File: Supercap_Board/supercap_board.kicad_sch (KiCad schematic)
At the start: 15 parts, among them Q10 2SCR587D3, Q11 2SAR587D3, U18 TLV9301xDBV

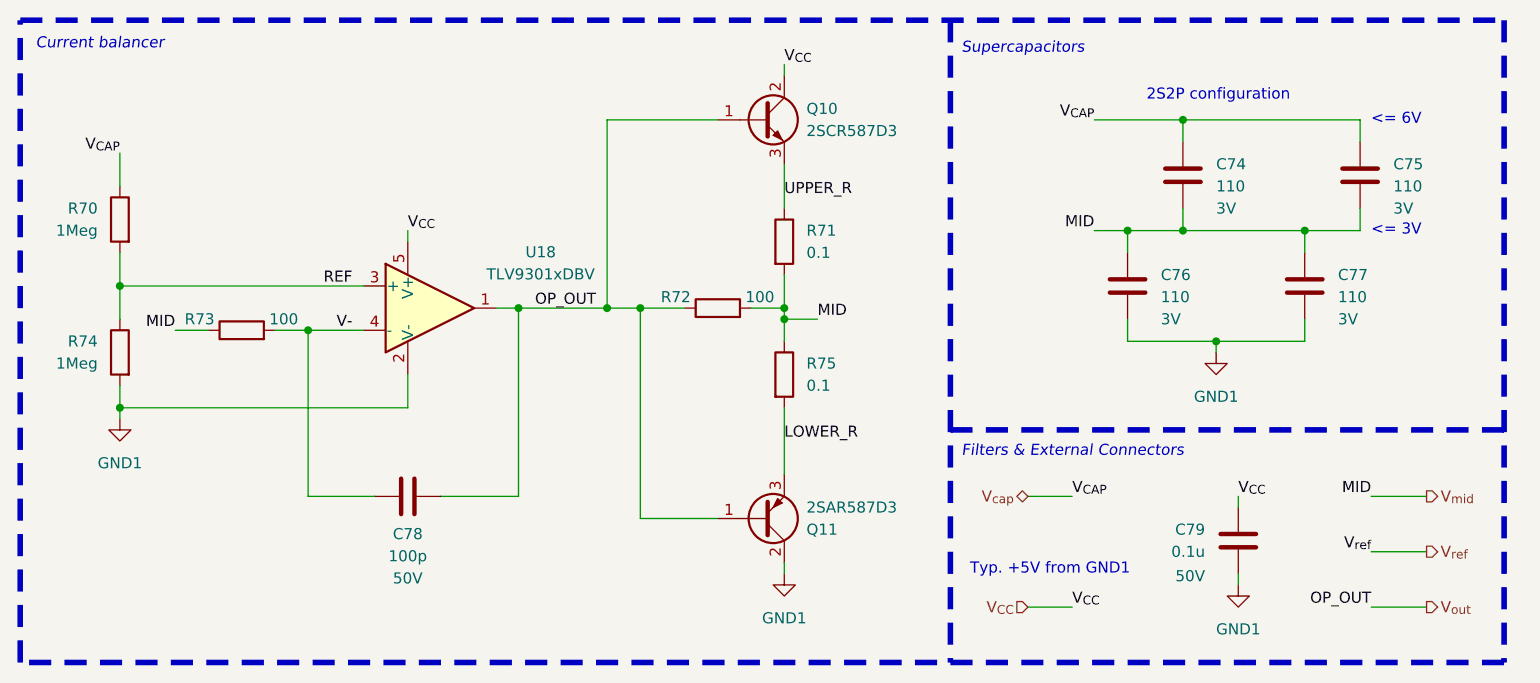
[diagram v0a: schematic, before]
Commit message: replaced 2p2s caps with full parallel
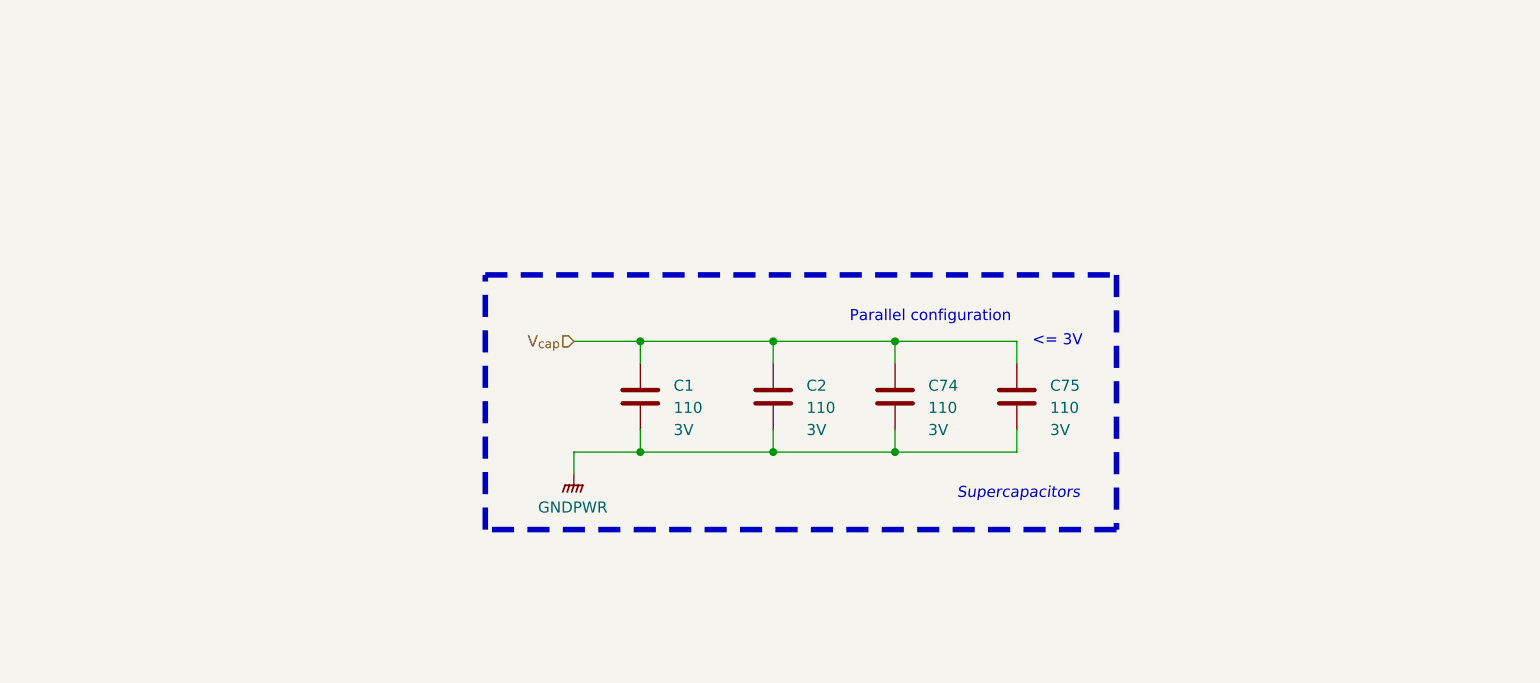
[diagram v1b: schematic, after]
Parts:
- removed C76, C77: 110, Capacitor_THT:C_Radial_D18.0mm_H35.5mm_P7.50mm, symbol Device:C
- removed C78: 100p, Capacitor_SMD:C_0603_1608Metric_Pad1.08x0.95mm_HandSolder, symbol Device:C
- removed C79: 0.1u, Capacitor_SMD:C_0603_1608Metric_Pad1.08x0.95mm_HandSolder, symbol Device:C
- removed Q10: 2SCR587D3, Package_TO_SOT_SMD:TO-252-2, symbol Transistor_BJT:Q_NPN_BCE
- removed Q11: 2SAR587D3, Package_TO_SOT_SMD:TO-252-2, symbol Transistor_BJT:Q_PNP_BCE
- removed R70, R74: 1Meg, Resistor_SMD:R_0603_1608Metric_Pad0.98x0.95mm_HandSolder, symbol Device:R
- removed R71, R75: 0.1, Resistor_SMD:R_1206_3216Metric_Pad1.30x1.75mm_HandSolder, symbol Device:R
- removed R72, R73: 100, Resistor_SMD:R_0603_1608Metric_Pad0.98x0.95mm_HandSolder, symbol Device:R
- removed U18: TLV9301xDBV, Package_TO_SOT_SMD:SOT-23-5_HandSoldering, symbol Amplifier_Operational:TLV9301xDBV
- added C1, C2: 110, Capacitor_THT:C_Radial_D18.0mm_H35.5mm_P7.50mm, symbol Device:C
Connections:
- net V_{cap}: now also C1.1, C2.1
- net V_{mid} renamed GNDPWR
- net GNDPWR: now also C1.2, C2.2
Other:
- note added: "Parallel configuration"
- note removed: "2S2P configuration"
- note removed: "<= 6V"
- note removed: "Current balancer"
- note removed: "Filters & External Connectors"
- note removed: "Typ. +5V from GND1"
- moved on the sheet: C74, C75
